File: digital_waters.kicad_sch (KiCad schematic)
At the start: 9 parts, among them U1 MCP3208, U2 M24C02-FMN

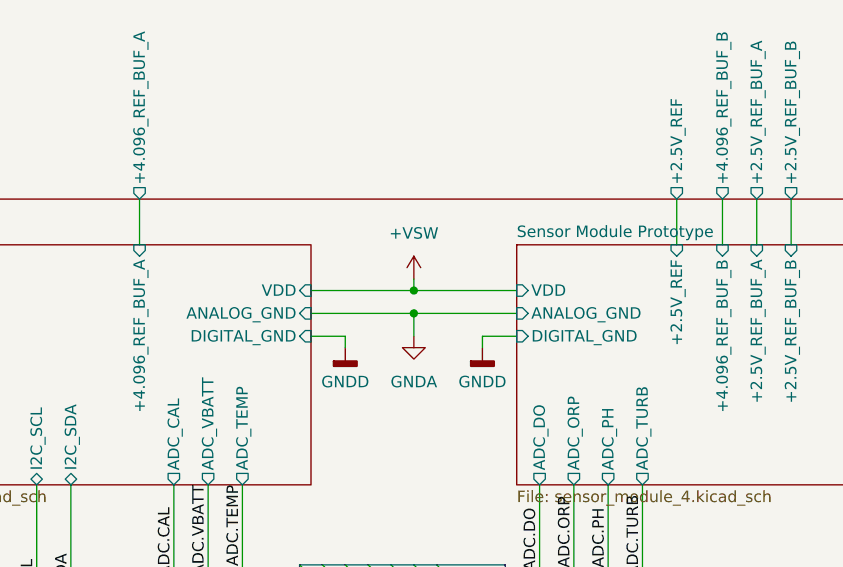
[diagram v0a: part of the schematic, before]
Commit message: BUG_FIX ------- - Swapped ground for the 2.5V reference on the non-inverting leg of U11B (External temperature probe)   This is due to the fact that the temp probe voltage can go both above and below the reference point so we need something higher than ground to prevent pegging the output to 0 when temp probe impedance drops below 1k.
FEATURES
--------
- Finalized many of the parts for the BOM
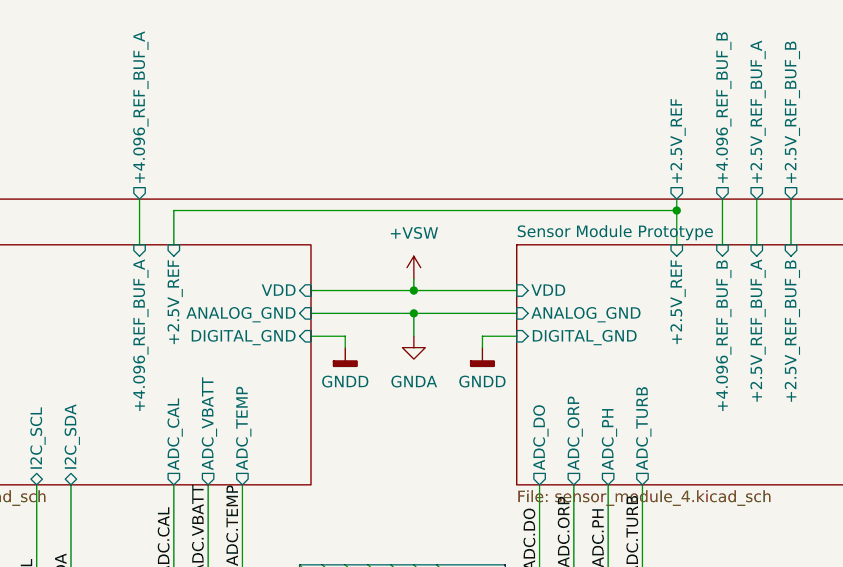
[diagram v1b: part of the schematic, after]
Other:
- sheet Base_Sensor ports: added +2.5V_REF; removed none
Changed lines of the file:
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@@
 	)
 	(junction
+		(at 138.43 41.91)
+		(diameter 0)
+		(color 0 0 0 0)
+	)
+	(junction
 		(at 134.62 113.03)
 		(diameter 0)
@@
 	(wire
 		(pts
+			(xy 138.43 40.64) (xy 138.43 41.91)
+		)
+		(stroke
+			(width 0)
+			(type default)
+		)
+	)
+	(wire
+		(pts
 			(xy 232.41 139.7) (xy 246.38 139.7)
 		)
@@
 	(wire
 		(pts
+			(xy 82.55 41.91) (xy 138.43 41.91)
+		)
+		(stroke
+			(width 0)
+			(type default)
+		)
+	)
+	(wire
+		(pts
 			(xy 259.08 128.27) (xy 259.08 130.81)
 		)
@@
 	(wire
 		(pts
-			(xy 273.05 140.97) (xy 273.05 148.59)
+			(xy 138.43 41.91) (xy 138.43 45.72)
 		)
 		(stroke
@@
 	(wire
 		(pts
-			(xy 187.96 118.11) (xy 187.96 125.73)
+			(xy 273.05 140.97) (xy 273.05 148.59)
 		)
 		(stroke
@@
 		)
 	)
-	(bus
+	(wire
 		(pts
-			(xy 119.38 85.09) (xy 120.65 85.09)
+			(xy 187.96 118.11) (xy 187.96 125.73)
 		)
 		(stroke
@@
 		)
 	)
-	(wire
+	(bus
 		(pts
-			(xy 33.02 25.4) (xy 33.02 19.05)
+			(xy 119.38 85.09) (xy 120.65 85.09)
 		)
 		(stroke
@@
 	(wire
 		(pts
-			(xy 106.68 83.82) (xy 106.68 92.71)
+			(xy 33.02 25.4) (xy 33.02 19.05)
 		)
 		(stroke
@@
 	(wire
 		(pts
-			(xy 134.62 113.03) (xy 143.51 113.03)
+			(xy 106.68 83.82) (xy 106.68 92.71)
 		)
 		(stroke
@@
 	(wire
 		(pts
-			(xy 138.43 40.64) (xy 138.43 45.72)
+			(xy 134.62 113.03) (xy 143.51 113.03)
 		)
 		(stroke
@@
 	(wire
 		(pts
+			(xy 82.55 45.72) (xy 82.55 41.91)
+		)
+		(stroke
+			(width 0)
+			(type default)
+		)
+	)
+	(wire
+		(pts
 			(xy 184.15 24.13) (xy 184.15 29.21)
 		)
@@
 			)
 		)
+		(property "Resistance" ""
+			(at 149.86 109.22 0)
+			(effects
+				(font
+					(size 1.27 1.27)
+				)
+				(hide yes)
+			)
+		)
 		(pin "1"
 		)
@@
 			)
 		)
+		(property "Resistance" ""
+			(at 246.38 128.27 0)
+			(effects
+				(font
+					(size 1.27 1.27)
+				)
+				(hide yes)
+			)
+		)
 		(pin "6"
 		)
@@
 			)
 		)
+		(property "Resistance" ""
+			(at 187.96 114.3 0)
+			(effects
+				(font
+					(size 1.27 1.27)
+				)
+				(hide yes)
+			)
+		)
 		(pin "2"
 		)
@@
 			)
 		)
+		(property "Resistance" ""
+			(at 198.12 114.3 0)
+			(effects
+				(font
+					(size 1.27 1.27)
+				)
+				(hide yes)
+			)
+		)
 		(pin "2"
 		)
@@
 			)
 		)
+		(property "Resistance" ""
+			(at 273.05 137.16 0)
+			(effects
+				(font
+					(size 1.27 1.27)
+				)
+				(hide yes)
+			)
+		)
 		(pin "1"
 		)
@@
 			)
 		)
+		(property "Resistance" ""
+			(at 143.51 109.22 0)
+			(effects
+				(font
+					(size 1.27 1.27)
+				)
+				(hide yes)
+			)
+		)
 		(pin "1"
 		)
@@
 			)
 		)
+		(property "Resistance" ""
+			(at 265.43 137.16 0)
+			(effects
+				(font
+					(size 1.27 1.27)
+				)
+				(hide yes)
+			)
+		)
 		(pin "1"
 		)
@@
 			)
 		)
+		(property "Resistance" ""
+			(at 134.62 109.22 0)
+			(effects
+				(font
+					(size 1.27 1.27)
+				)
+				(hide yes)
+			)
+		)
 		(pin "1"
 		)
@@
 			)
 		)
+		(property "Resistance" ""
+			(at 106.68 107.95 0)
+			(effects
+				(font
+					(size 1.27 1.27)
+				)
+				(hide yes)
+			)
+		)
 		(pin "7"
 		)
@@
 			(effects
 				(font
+					(size 1.27 1.27)
+				)
+				(justify right)
+			)
+		)
+		(pin "+2.5V_REF" input
+			(at 82.55 45.72 90)
+			(effects
+				(font
